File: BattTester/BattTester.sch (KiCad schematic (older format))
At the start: 22 parts, among them J1 Battery, J2 SD_Card, J3 PWR, J4 UPDI, U1 LT1286CN8, U2 ATtiny1624-SS, U3 LD1086DT33

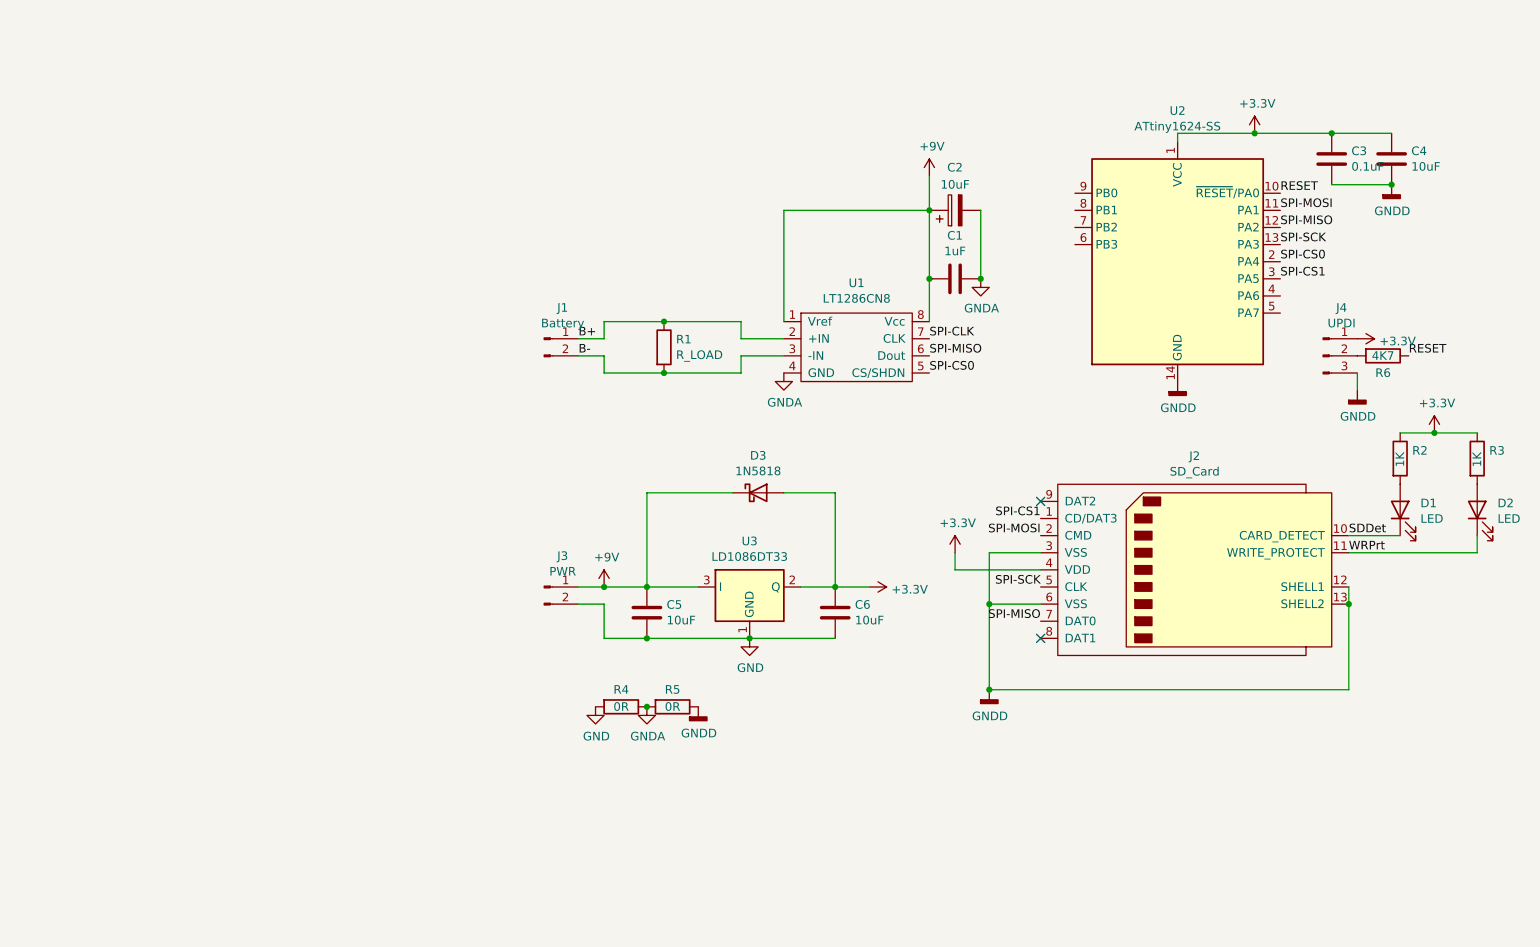
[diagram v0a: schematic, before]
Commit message: Constant current load
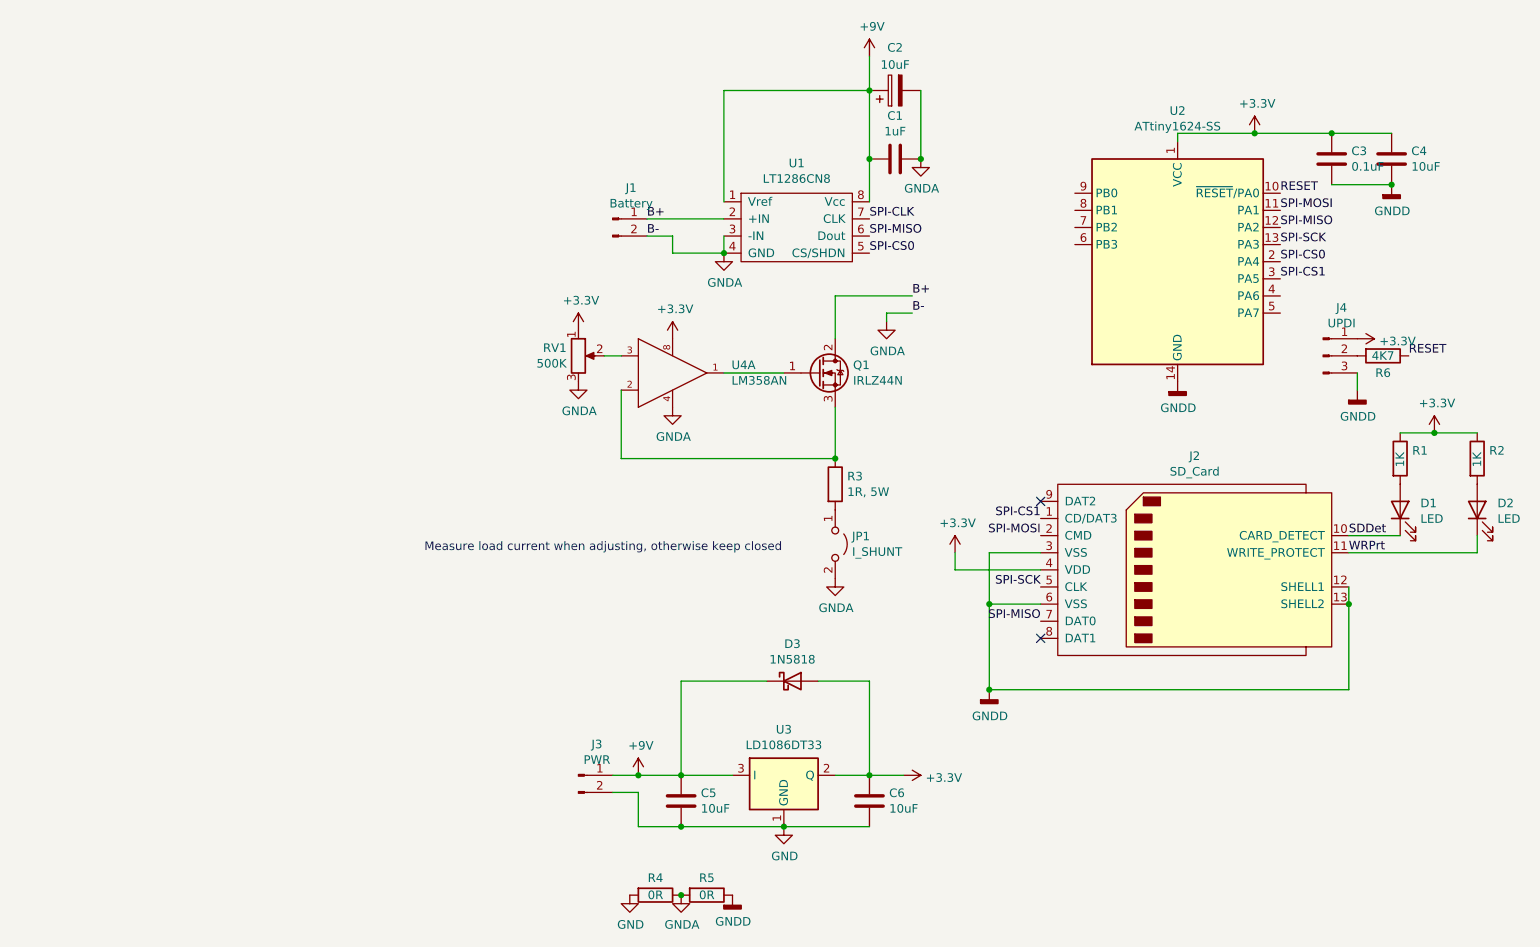
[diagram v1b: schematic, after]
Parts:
- removed R1: R_LOAD, symbol Device:R
- added JP1: I_SHUNT, Connector_PinHeader_2.54mm:PinHeader_1x02_P2.54mm_Vertical, symbol Jumper:Jumper_2_Open
- added Q1: IRLZ44N, Package_TO_SOT_THT:TO-220-3_Vertical, symbol Transistor_FET:IRLZ44N
- added R3: 1R, 5W, Resistor_THT:R_Axial_Power_L48.0mm_W12.5mm_P55.88mm, symbol Device:R
- added RV1: 500K, Connector_PinHeader_2.54mm:PinHeader_1x03_P2.54mm_Vertical, symbol Device:R_POT
- added U4: LM358AN, BattTester:Texas_Instruments-P0008A-0-0-MFG, symbol LM358AN:LM358AN_NOPB
- C1, C3, C4, C5, C6: footprint (none) -> Capacitor_SMD:C_0805_2012Metric_Pad1.18x1.45mm_HandSolder
- C2: footprint (none) -> Capacitor_SMD:C_1206_3216Metric_Pad1.33x1.80mm_HandSolder
- D1, D2: footprint (none) -> LED_SMD:LED_0805_2012Metric_Pad1.15x1.40mm_HandSolder
- D3: footprint (none) -> Diode_THT:D_DO-15_P10.16mm_Horizontal
- J1: footprint (none) -> Connector_PinHeader_2.54mm:PinHeader_1x02_P2.54mm_Horizontal
- J2: footprint (none) -> Connector_Card:SD_TE_2041021
- J3: footprint (none) -> Connector_PinHeader_2.54mm:PinHeader_1x02_P2.54mm_Vertical
- J4: footprint (none) -> Connector_PinHeader_2.54mm:PinHeader_1x03_P2.54mm_Vertical
- R1: renamed from R2; footprint (none) -> Resistor_SMD:R_1206_3216Metric_Pad1.30x1.75mm_HandSolder
- R2: renamed from R3; footprint (none) -> Resistor_SMD:R_1206_3216Metric_Pad1.30x1.75mm_HandSolder
- R4, R5, R6: footprint (none) -> Resistor_SMD:R_1206_3216Metric_Pad1.30x1.75mm_HandSolder
- U1: footprint (none) -> BattTester:Texas_Instruments-P0008A-0-0-MFG
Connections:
- net B- is gone; now on net GNDA: J1.2 (Pin_2), U1.3 (-IN)
- net +3V3: now also RV1.1, U4.8 (V+)
- net B+: now also Q1.2 (D)
- net GNDA: now also JP1.2 (B), RV1.3, U4.4 (GND)
- new net: RV1.2, U4.3 (NON-INVERTING_INPUT_A)
- new net: Q1.1 (G), U4.1 (OUTPUT_A)
- new net: Q1.3 (S), R3.1, U4.2 (INVERTING_INPUT_A)
- new net: JP1.1 (A), R3.2
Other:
- note added: "Measure load current when adjusting, otherwise keep closed"
- moved on the sheet: C1, C2, C5, C6, D3, J1, J3, R4, R5, U1, U3

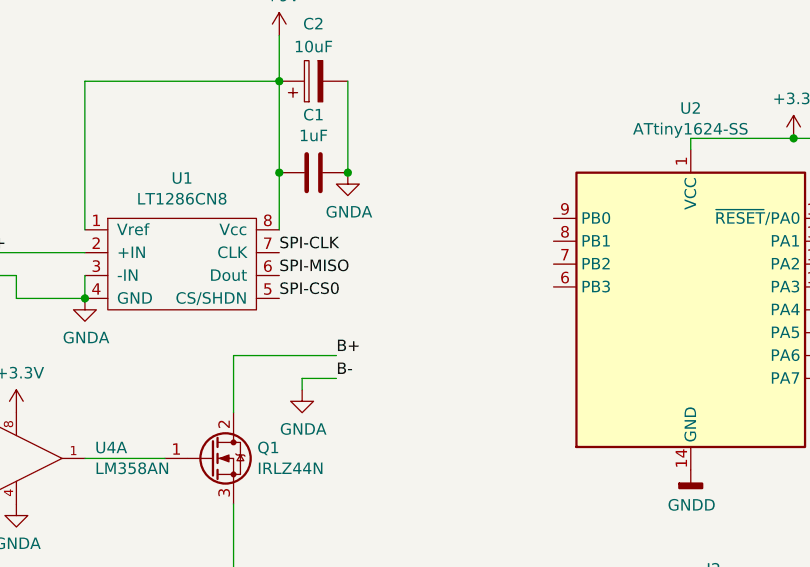
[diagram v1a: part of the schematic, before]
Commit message: level shifter placeholder
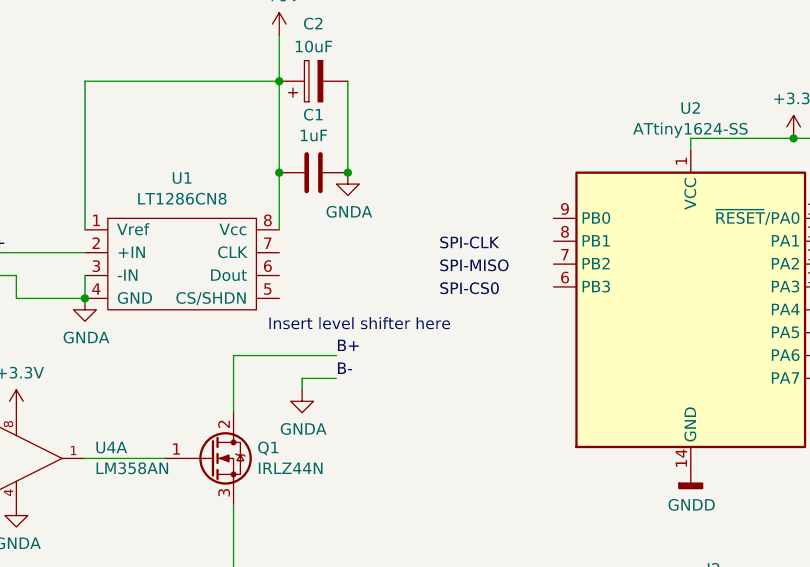
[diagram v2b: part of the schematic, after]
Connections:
- net SPI-CLK: no longer U1.7 (CLK)
- net SPI-CS0: no longer U1.5 (CS/SHDN)
- net SPI-MISO: no longer U1.6 (Dout)
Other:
- note added: "Insert level shifter here"
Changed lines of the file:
@@
 	1    0    0    -1
 $EndComp
-Text Label 5500 1700 0    50   ~ 0
+Text Label 6200 1700 0    50   ~ 0
 SPI-CLK
-Text Label 5500 1800 0    50   ~ 0
+Text Label 6200 1800 0    50   ~ 0
 SPI-MISO
-Text Label 5500 1900 0    50   ~ 0
+Text Label 6200 1900 0    50   ~ 0
 SPI-CS0
 $Comp
@@
 Text Notes 2900 3650 0    50   ~ 0
 Measure load current when adjusting, otherwise keep closed
+Text Notes 5450 2050 0    50   ~ 0
+Insert level shifter here
 $EndSCHEMATC

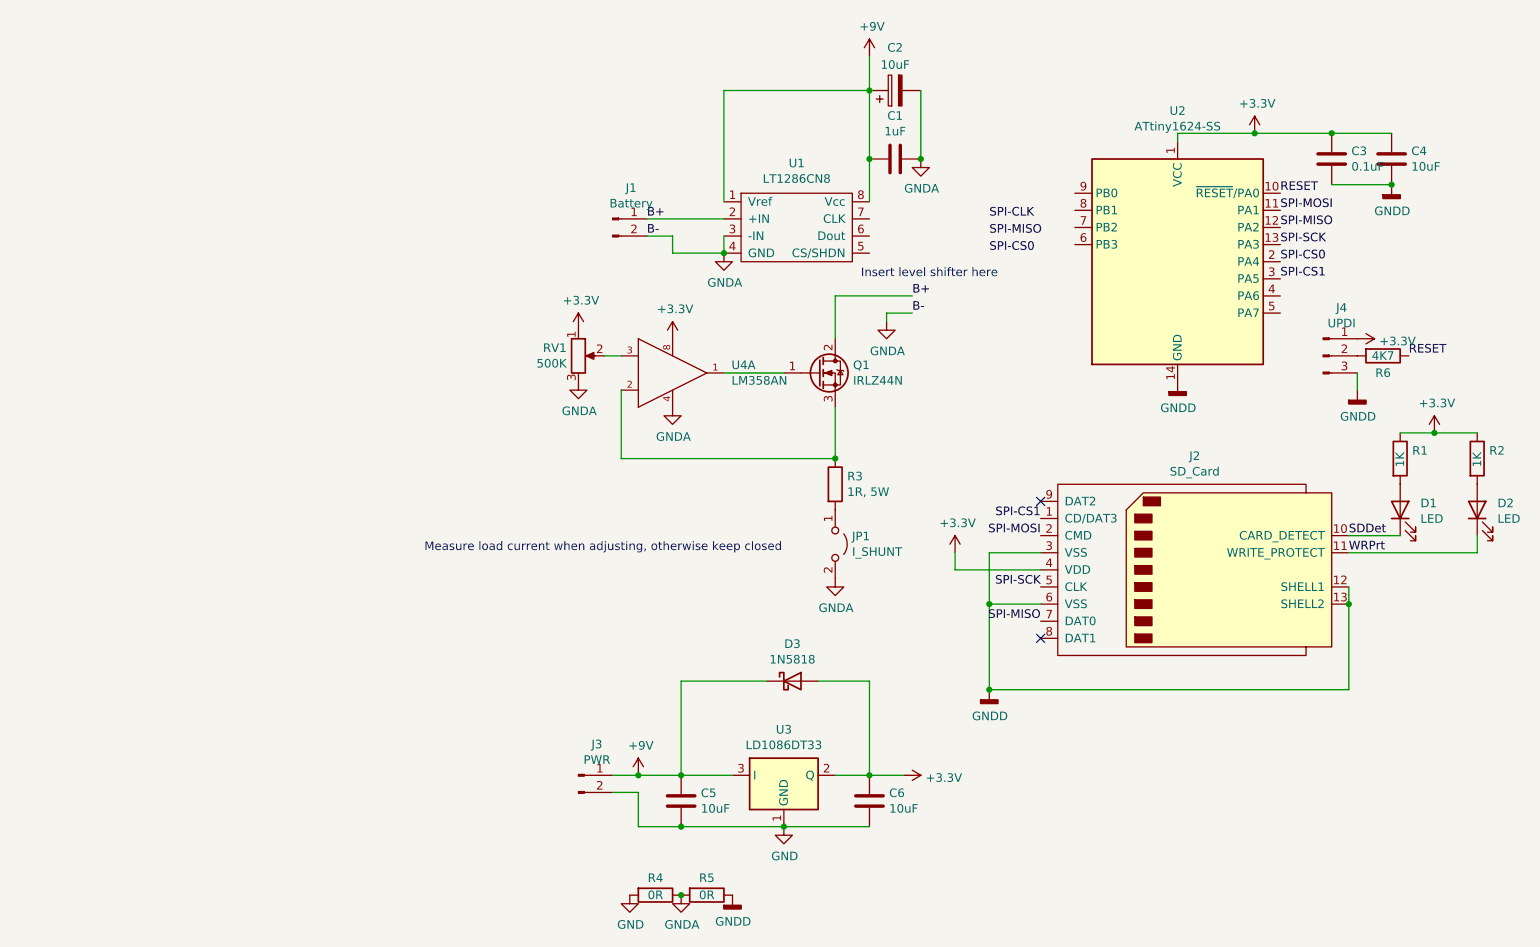
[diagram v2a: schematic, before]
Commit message: Clean up schematic, add level shifter breakout
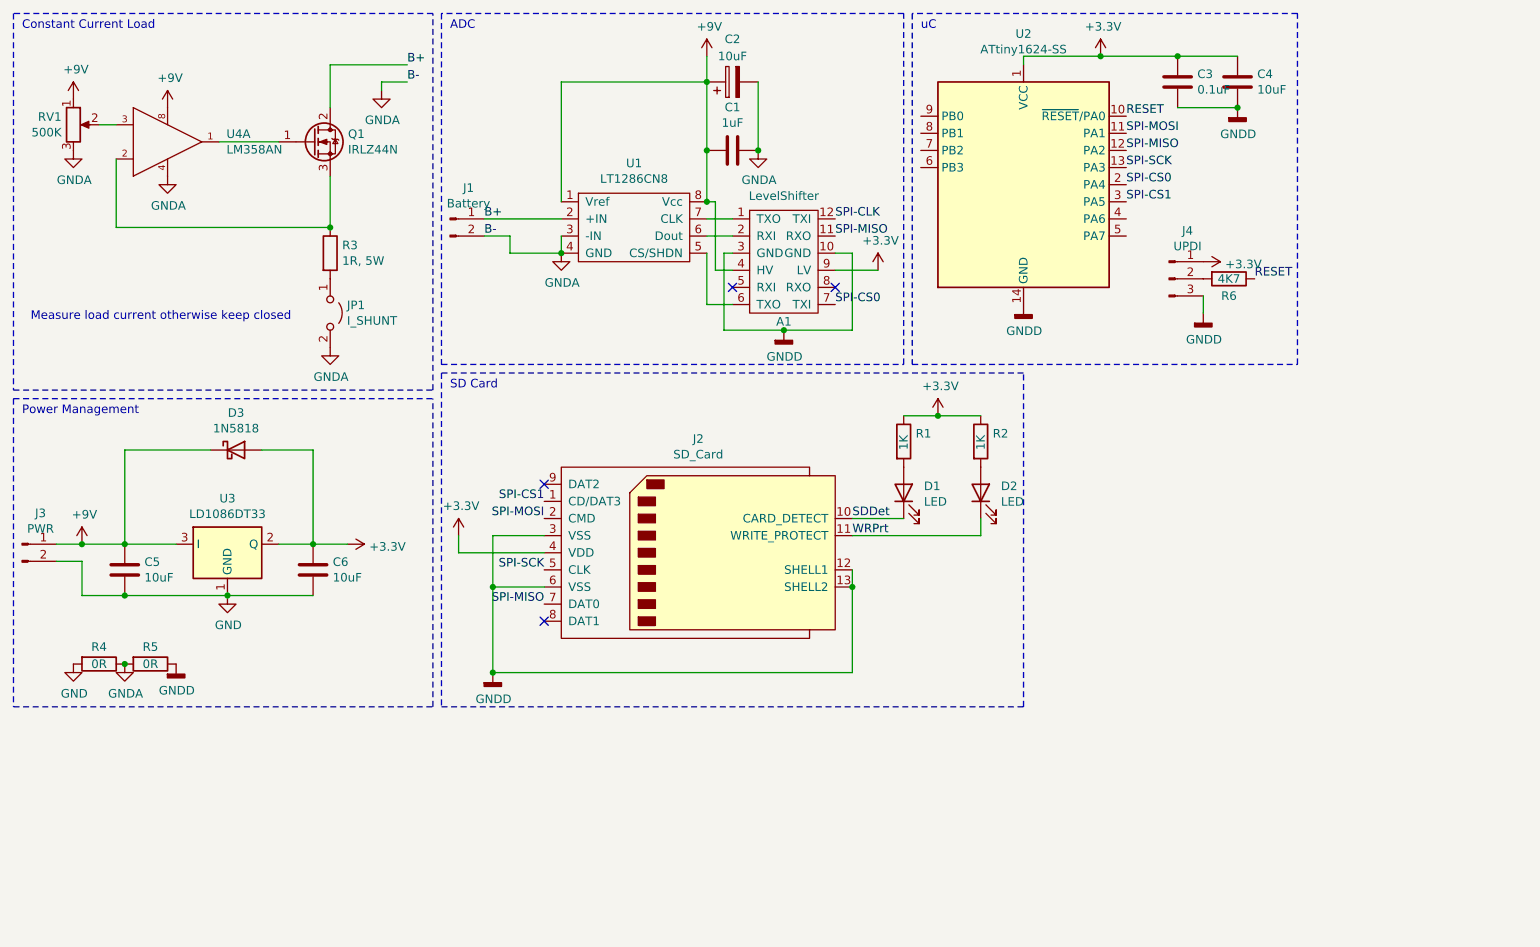
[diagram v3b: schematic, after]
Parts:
- added A1: LevelShifter, BattTester:LevelShifterBreakout, symbol BattTester:LevelShifter
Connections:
- net +3V3: now also A1.9 (LV); no longer RV1.1, U4.8 (V+)
- net +9V: now also RV1.1, U4.8 (V+), A1.4 (HV)
- net GNDD: now also A1.10 (GND), A1.3 (GND)
- net SPI-CLK: now also A1.12 (TXI)
- net SPI-CS0: now also A1.7 (TXI)
- net SPI-MISO: now also A1.11 (RXO)
- net at U1.5 (CS/SHDN): now also A1.6 (TXO)
- net at U1.6 (Dout): now also A1.2 (RXI)
- net at U1.7 (CLK): now also A1.1 (TXO)
- no-connect marks 2 -> 4
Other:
- note added: "ADC"
- note added: "Constant Current Load"
- note added: "Measure load current otherwise keep closed"
- note added: "Power Management"
- note added: "SD Card"
- note added: "uC"
- note removed: "Insert level shifter here"
- note removed: "Measure load current when adjusting, otherwise keep closed"
- moved on the sheet: C1, C2, C3, C4, C5, C6, D1, D2, D3, J1, J2, J3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

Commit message: grounding
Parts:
- removed R4, R5: 0R, Resistor_SMD:R_1206_3216Metric_Pad1.30x1.75mm_HandSolder, symbol Device:R
- J1: footprint Connector_PinHeader_2.54mm:PinHeader_1x02_P2.54mm_Horizontal -> Connector_PinHeader_2.54mm:PinHeader_1x02_P2.54mm_Vertical
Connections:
- net GNDA is gone; now on net GND: C1.1, C2.2, J1.2 (Pin_2), JP1.2 (B), RV1.3, U1.3 (-IN), U1.4 (GND), U4.4 (GND)
- net GNDD is gone; now on net GND: A1.10 (GND), A1.3 (GND), C3.2, C4.2, J2.12 (SHELL1), J2.13 (SHELL2), J2.3 (VSS), J2.6 (VSS), J4.3 (Pin_3), U2.14 (GND)
- net SPI-CLK is gone; now on net SPI-SCK: A1.12 (TXI)
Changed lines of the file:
@@
 F 0 "J1" H 3158 1881 50  0000 C CNN
 F 1 "Battery" H 3158 1790 50  0000 C CNN
-F 2 "Connector_PinHeader_2.54mm:PinHeader_1x02_P2.54mm_Horizontal" H 3050 1700 50  0001 C CNN
+F 2 "Connector_PinHeader_2.54mm:PinHeader_1x02_P2.54mm_Vertical" H 3050 1700 50  0001 C CNN
 F 3 "~" H 3050 1700 50  0001 C CNN
 	1    3050 1700
@@
 $EndComp
 Text Label 5300 1700 0    50   ~ 0
-SPI-CLK
+SPI-SCK
 Text Label 5300 1800 0    50   ~ 0
 SPI-MISO
@@
 	1    0    0    -1
 $EndComp
-$Comp
-L Device:R R4
-U 1 1 616F2096
-P 1000 4300
-F 0 "R4" V 900 4300 50  0000 C CNN
-F 1 "0R" V 1000 4300 50  0000 C CNN
-F 2 "Resistor_SMD:R_1206_3216Metric_Pad1.30x1.75mm_HandSolder" V 930 4300 50  0001 C CNN
-F 3 "~" H 1000 4300 50  0001 C CNN
-	1    1000 4300
-	0    1    1    0
-$EndComp
-$Comp
-L Device:R R5
-U 1 1 616F313F
-P 1300 4300
-F 0 "R5" V 1200 4300 50  0000 C CNN
-F 1 "0R" V 1300 4300 50  0000 C CNN
-F 2 "Resistor_SMD:R_1206_3216Metric_Pad1.30x1.75mm_HandSolder" V 1230 4300 50  0001 C CNN
-F 3 "~" H 1300 4300 50  0001 C CNN
-	1    1300 4300
-	0    1    1    0
-$EndComp
-Connection ~ 1150 4300
 $Comp
 L Regulator_Linear:IFX27001TFV33 U3
@@
 $EndComp
 Connection ~ 2350 1750
-$Comp
-L power:GNDA #PWR0122
-U 1 1 61738E8E
-P 2350 2450
-F 0 "#PWR0122" H 2350 2200 50  0001 C CNN
-F 1 "GNDA" H 2355 2277 50  0000 C CNN
-F 2 "" H 2350 2450 50  0001 C CNN
-F 3 "" H 2350 2450 50  0001 C CNN
-	1    2350 2450
-	1    0    0    -1
-$EndComp
 Wire Wire Line
 	2350 1050 2350 800
@@
 Wire Notes Line
 	8000 500  5750 500
+Wire Wire Line
+	1450 4300 1150 4300
+Connection ~ 1150 4300
+Wire Wire Line
+	1150 4300 850  4300
+$Comp
+L power:GNDD #PWR0122
+U 1 1 6178CCE3
+P 2350 2450
+F 0 "#PWR0122" H 2350 2200 50  0001 C CNN
+F 1 "GNDD" H 2354 2295 50  0000 C CNN
+F 2 "" H 2350 2450 50  0001 C CNN
+F 3 "" H 2350 2450 50  0001 C CNN
+	1    2350 2450
+	1    0    0    -1
+$EndComp
 $EndSCHEMATC

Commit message: Finish routing
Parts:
- U1, U4: footprint BattTester:Texas_Instruments-P0008A-0-0-MFG -> BattTester:DIP8
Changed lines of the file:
@@
 F 0 "U4" H 1744 1096 50  0000 L CNN
 F 1 "LM358AN" H 1744 1005 50  0000 L CNN
-F 2 "BattTester:Texas_Instruments-P0008A-0-0-MFG" H 1100 1550 50  0001 L CNN
+F 2 "BattTester:DIP8" H 1100 1550 50  0001 L CNN
 F 3 "http://www.ti.com/lit/ds/symlink/lm358-n.pdf" H 1100 1650 50  0001 L CNN
 F 4 "No" H 1100 1750 50  0001 L CNN "automotive"
@@
 F 0 "U1" H 4125 1525 50  0000 C CNN
 F 1 "LT1286CN8" H 4125 1434 50  0000 C CNN
-F 2 "BattTester:Texas_Instruments-P0008A-0-0-MFG" H 4150 1450 50  0001 C CNN
+F 2 "BattTester:DIP8" H 4150 1450 50  0001 C CNN
 F 3 "" H 4150 1450 50  0001 C CNN
 	1    4150 1450

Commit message: minor name fix
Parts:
- U1: value LT1286CN8 -> LTC1286CN8
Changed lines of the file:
@@
 P 4150 1450
 F 0 "U1" H 4125 1525 50  0000 C CNN
-F 1 "LT1286CN8" H 4125 1434 50  0000 C CNN
+F 1 "LTC1286CN8" H 4125 1434 50  0000 C CNN
 F 2 "BattTester:DIP8" H 4150 1450 50  0001 C CNN
 F 3 "" H 4150 1450 50  0001 C CNN
